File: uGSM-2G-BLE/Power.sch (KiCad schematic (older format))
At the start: 11 parts

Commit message: power
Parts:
- added C? (x3): 100nF, Capacitor_SMD:C_0603_1608Metric, symbol Device:C
- added C?: 1uF, Capacitor_SMD:C_0603_1608Metric, symbol Device:C
- added C?: 2.2uF, Capacitor_SMD:C_0603_1608Metric, symbol Device:C
- added C?: 10uF, Capacitor_SMD:C_0603_1608Metric, symbol Device:C
- added D?: D, symbol Device:D
- added D?: PRTR5V0U2X, Package_TO_SOT_SMD:SOT-143, symbol Power_Protection:PRTR5V0U2X
- added J?: VCC_INPUT, symbol Connector:Screw_Terminal_01x02
- added J?: USB_B_Micro, symbol Connector:USB_B_Micro
- added U?: MIC5225-3.3YM5-TR, Package_TO_SOT_SMD:SOT-23-5, symbol Regulator_Linear:MIC5205-3.3YM5
- U?: Manufacturerpart (none) -> TPS562201DDCR
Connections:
- net GND: now also C?.2, C?.2, C?.2, C?.2, C?.2, C?.2, D?.1 (GND), J?.1 (Pin_1), J?.5 (GND), J?.6 (Shield), U?.2 (GND)
- net SIM_VCC: now also C?.1, U?.1 (IN), U?.3 (EN)
- net VCC: now also D?.1 (K), J?.2 (Pin_2)
- new net 3V3: C?.1, U?.5 (OUT)
- new net USB_5V: C?.1, C?.1, C?.1, C?.1, D?.2 (A), D?.4 (VCC), J?.1 (VBUS)
- new net USB_D+: D?.3 (I/O2), J?.3 (D+)
- new net USB_D-: D?.2 (I/O1), J?.2 (D-)
- no-connect marks 0 -> 2
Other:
- note added: "Atleast 16V rated cap"
- note added: "Follow classic USB guidelines"
- note added: "May change! Check issue on github"
- note added: "R1 and R2 +/- 1%\n"

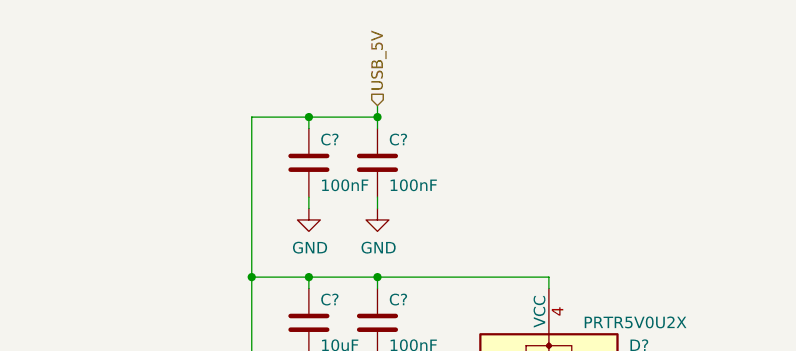
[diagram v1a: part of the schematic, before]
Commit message: ble connected to mikrobus
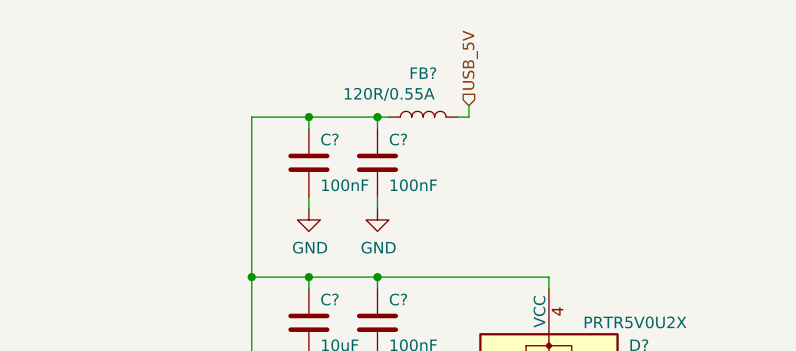
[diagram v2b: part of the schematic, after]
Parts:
- added FB?: 120R/0.55A, symbol Device:L
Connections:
- net USB_5V: now also FB?.2; no longer C?.1, C?.1, C?.1, C?.1, D?.4 (VCC), J?.1 (VBUS)
- new net: C?.1, C?.1, C?.1, C?.1, D?.4 (VCC), FB?.1, J?.1 (VBUS)
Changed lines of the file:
@@
 $Descr A4 11693 8268
 encoding utf-8
-Sheet 3 6
+Sheet 2 6
 Title ""
 Date ""
@@
 $EndComp
 $Comp
-L power:GND #PWR?
-U 1 1 5E5196D5
-P 8450 3750
-F 0 "#PWR?" H 8450 3500 50  0001 C CNN
-F 1 "GND" H 8455 3577 50  0000 C CNN
-F 2 "" H 8450 3750 50  0001 C CNN
-F 3 "" H 8450 3750 50  0001 C CNN
-	1    8450 3750
-	1    0    0    -1
-$EndComp
-Wire Wire Line
-	8400 3650 8400 3700
-Wire Wire Line
-	8400 3700 8450 3700
-Wire Wire Line
-	8500 3700 8500 3650
-Wire Wire Line
-	8450 3700 8450 3750
-Connection ~ 8450 3700
-Wire Wire Line
-	8450 3700 8500 3700
-$Comp
 L Power_Protection:PRTR5V0U2X D?
 U 1 1 5E51C285
@@
 Wire Wire Line
 	8850 1050 9100 1050
-Wire Wire Line
-	9400 1050 9400 1000
 Connection ~ 8850 1750
 Wire Wire Line
 	9400 1050 9400 1100
-Connection ~ 9400 1050
 Wire Wire Line
 	9100 1050 9100 1100
@@
 Wire Wire Line
 	9400 1400 9400 1450
-Text HLabel 9400 1000 1    50   Input ~ 0
+Text HLabel 9800 1000 1    50   Input ~ 0
 USB_5V
 Text Notes 9650 3500 0    50   ~ 0
@@
 Wire Wire Line
 	5650 3550 5700 3550
+$Comp
+L Device:L FB?
+U 1 1 5E54216F
+P 9600 1050
+F 0 "FB?" V 9790 1050 50  0000 C CNN
+F 1 "120R/0.55A" V 9700 1200 50  0000 C CNN
+F 2 "" H 9600 1050 50  0001 C CNN
+F 3 "~" H 9600 1050 50  0001 C CNN
+	1    9600 1050
+	0    -1   -1   0
+$EndComp
+Wire Wire Line
+	9450 1050 9400 1050
+Connection ~ 9400 1050
+Wire Wire Line
+	9750 1050 9800 1050
+Wire Wire Line
+	9800 1050 9800 1000
+Wire Wire Line
+	8450 3700 8500 3700
+Wire Wire Line
+	8500 3700 8500 3650
+Wire Wire Line
+	8400 3650 8400 3700
+$Comp
+L power:GND #PWR?
+U 1 1 5E5196D5
+P 8450 3750
+F 0 "#PWR?" H 8450 3500 50  0001 C CNN
+F 1 "GND" H 8455 3577 50  0000 C CNN
+F 2 "" H 8450 3750 50  0001 C CNN
+F 3 "" H 8450 3750 50  0001 C CNN
+	1    8450 3750
+	1    0    0    -1
+$EndComp
+Wire Wire Line
+	8450 3700 8450 3750
+Connection ~ 8450 3700
+Wire Wire Line
+	8400 3700 8450 3700
 $EndSCHEMATC

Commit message: completed all issues, updating
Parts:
- removed C? (x3): 100nF, Capacitor_SMD:C_0603_1608Metric, symbol Device:C
- removed C?: 1uF, Capacitor_SMD:C_0603_1608Metric, symbol Device:C
- removed C?: 2.2uF, Capacitor_SMD:C_0603_1608Metric, symbol Device:C
- removed C?: 10uF, Capacitor_SMD:C_0603_1608Metric, symbol Device:C
- removed D?: D, symbol Device:D
- removed D?: PRTR5V0U2X, Package_TO_SOT_SMD:SOT-143, symbol Power_Protection:PRTR5V0U2X
- removed FB?: 120R/0.55A, symbol Device:L
- removed J?: VCC_INPUT, symbol Connector:Screw_Terminal_01x02
- removed U?: MIC5225-3.3YM5-TR, Package_TO_SOT_SMD:SOT-23-5, symbol Regulator_Linear:MIC5205-3.3YM5
- added C? (x2): 10uF, Capacitor_SMD:C_0805_2012Metric, symbol Device:C
- added C? (x2): 100nF, Capacitor_SMD:C_0603_1608Metric, symbol Device:C
- added C?: 330pF, Capacitor_SMD:C_0603_1608Metric, symbol Device:C
- added D?: MBR120, Diode_SMD:D_SOD-123F, symbol Diode:MBR340
- added J?: PWR_INPUT, symbol Connector:Screw_Terminal_01x02
- added L?: BLM21PG220SN1D, Inductor_SMD:L_0805_2012Metric, symbol Device:L
- added Q?: DMG2305, Package_TO_SOT_SMD:SOT-23, symbol Transistor_FET:DMG2301L
- added R? (x2): 100K, Resistor_SMD:R_0603_1608Metric, symbol Device:R
- added R?: 1M, Resistor_SMD:R_0603_1608Metric, symbol Device:R
- added R? (x2): 27, Resistor_SMD:R_0603_1608Metric, symbol Device:R
- added U?: AP2112K-3.3, Package_TO_SOT_SMD:SOT-23-5, symbol Regulator_Linear:AP2112K-3.3
- added U?: USBLC6-2SC6, Package_TO_SOT_SMD:SOT-23-6, symbol Power_Protection:USBLC6-2SC6
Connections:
- net 3V3: now also C?.1, U?.5 (VOUT)
- net GND: now also C?.1, C?.1, C?.1, C?.2, C?.2, J?.1 (Pin_1), R?.1, R?.1, U?.2 (GND), U?.2 (GND); no longer J?.6 (Shield)
- net USB_5V: now also C?.2, D?.2 (A), L?.1, Q?.1 (G), R?.2, U?.5 (VBUS)
- net USB_D+: now also R?.2; no longer J?.3 (D+)
- net USB_D-: now also R?.2; no longer J?.2 (D-)
- net VCC: now also C?.1, D?.1 (K), Q?.2 (S), R?.2, U?.1 (VIN)
- net at J?.1 (VBUS): now also C?.2, L?.2
- new net: C?.2, J?.6 (Shield), R?.2
- new net: R?.1, U?.3 (EN)
- new net: R?.1, U?.4 (IO2)
- new net: R?.1, U?.6 (IO1)
- new net PWR_USB_D+: J?.3 (D+), U?.3 (IO2)
- new net PWR_USB_D-: J?.2 (D-), U?.1 (IO1)
- new net RAW_PWR_IN: J?.2 (Pin_2), Q?.3 (D)
- no-connect marks 2 -> 1
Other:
- note added: "select footprint\n"
- note removed: "Atleast 16V rated cap"
- note removed: "Follow classic USB guidelines"
- note removed: "May change! Check issue on github"
- moved on the sheet: J?

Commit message: added all email issue correction
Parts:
- removed Q?: DMG2305, Package_TO_SOT_SMD:SOT-23, symbol Transistor_FET:DMG2301L
- removed R?: 27, Resistor_SMD:R_0603_1608Metric, symbol Device:R
- removed U?: USBLC6-2SC6, Package_TO_SOT_SMD:SOT-23-6, symbol Power_Protection:USBLC6-2SC6
- added Q?: DMG2305, Package_TO_SOT_SMD:SOT-23, symbol Transistor_FET:SUD08P06-155L
- added R?: 27, Resistor_SMD:R_0603_1608Metric, symbol Device:R
- added U?: USBLC6, symbol ugsm_lib:USBLC6
- R?: value 100K -> 10K
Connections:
- net GND: now also U?.2 (GND)
- net PWR_USB_D+: now also U?.3 (INPUT2)
- net PWR_USB_D-: now also U?.1 (INPUT1)
- net RAW_PWR_IN: now also Q?.2 (D)
- net USB_5V: now also Q?.1 (G), U?.5 (VCC)
- net USB_D+: now also R?.2
- net VCC: now also Q?.3 (S)
- net at R?.1: now also U?.6 (OUTPUT1)
- new net: R?.1, U?.4 (OUTPUT2)
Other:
- moved on the sheet: R?
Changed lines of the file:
@@
 $EndComp
 NoConn ~ 7600 1950
-Text HLabel 9000 1350 1    50   Input ~ 0
+Text HLabel 10800 1700 2    50   Input ~ 0
 USB_D-
-Text HLabel 10100 1400 1    50   Input ~ 0
+Text HLabel 10800 1850 2    50   Input ~ 0
 USB_D+
 Text HLabel 8600 1500 1    50   Input ~ 0
@@
 3V3
 $Comp
-L Transistor_FET:DMG2301L Q?
-U 1 1 5E80CE9A
-P 1300 3600
-F 0 "Q?" H 1504 3646 50  0000 L CNN
-F 1 "DMG2305" H 1504 3555 50  0000 L CNN
-F 2 "Package_TO_SOT_SMD:SOT-23" H 1500 3525 50  0001 L CIN
-F 3 "https://www.diodes.com/assets/Datasheets/DMG2305UX.pdf" H 1300 3600 50  0001 L CNN
-	1    1300 3600
-	1    0    0    -1
-$EndComp
-$Comp
 L Diode:MBR340 D?
 U 1 1 5E80DF50
@@
 P 1000 4300
 F 0 "R?" H 950 4350 50  0000 R CNN
-F 1 "100K" H 950 4450 50  0000 R CNN
+F 1 "10K" H 950 4450 50  0000 R CNN
 F 2 "Resistor_SMD:R_0603_1608Metric" V 930 4300 50  0001 C CNN
 F 3 "~" H 1000 4300 50  0001 C CNN
@@
 Text GLabel 1400 3250 1    50   Input ~ 0
 RAW_PWR_IN
-$Comp
-L Power_Protection:USBLC6-2SC6 U?
-U 1 1 5E8934D8
-P 9550 1950
-F 0 "U?" H 9300 2300 50  0000 C CNN
-F 1 "USBLC6-2SC6" H 9950 1600 50  0000 C CNN
-F 2 "Package_TO_SOT_SMD:SOT-23-6" H 8800 2350 50  0001 C CNN
-F 3 "http://www2.st.com/resource/en/datasheet/CD00050750.pdf" H 9750 2300 50  0001 C CNN
-F 4 "https://export.farnell.com/stmicroelectronics/usblc6-2sc6/esd-protection-3-5pf-17v-sot23/dp/1269406?st=USBLC6-2" H 9550 1950 50  0001 C CNN "Farnell"
-	1    9550 1950
-	1    0    0    -1
-$EndComp
 $Comp
 L Device:C C?
@@
 L Device:R R?
 U 1 1 5E8A0288
-P 9000 1550
-F 0 "R?" H 8950 1600 50  0000 R CNN
-F 1 "27" H 8950 1700 50  0000 R CNN
-F 2 "Resistor_SMD:R_0603_1608Metric" V 8930 1550 50  0001 C CNN
-F 3 "~" H 9000 1550 50  0001 C CNN
-	1    9000 1550
-	-1   0    0    1
-$EndComp
-$Comp
-L Device:R R?
-U 1 1 5E8A077E
-P 10100 1600
-F 0 "R?" H 10050 1650 50  0000 R CNN
-F 1 "27" H 10050 1750 50  0000 R CNN
-F 2 "Resistor_SMD:R_0603_1608Metric" V 10030 1600 50  0001 C CNN
-F 3 "~" H 10100 1600 50  0001 C CNN
-	1    10100 1600
-	-1   0    0    1
+P 10600 1700
+F 0 "R?" V 10600 1750 50  0000 R CNN
+F 1 "27" V 10650 1600 50  0000 R CNN
+F 2 "Resistor_SMD:R_0603_1608Metric" V 10530 1700 50  0001 C CNN
+F 3 "~" H 10600 1700 50  0001 C CNN
+	1    10600 1700
+	0    -1   -1   0
 $EndComp
 Wire Wire Line
@@
 Wire Wire Line
 	8600 1550 8600 1500
-Text HLabel 9550 1400 1    50   Input ~ 0
+Text HLabel 9850 1400 1    50   Input ~ 0
 USB_5V
-$Comp
-L power:GND #PWR?
-U 1 1 5E8E108F
-P 9550 2500
-F 0 "#PWR?" H 9550 2250 50  0001 C CNN
-F 1 "GND" H 9555 2327 50  0000 C CNN
-F 2 "" H 9550 2500 50  0001 C CNN
-F 3 "" H 9550 2500 50  0001 C CNN
-	1    9550 2500
-	1    0    0    -1
-$EndComp
-Wire Wire Line
-	9550 1400 9550 1450
-Wire Wire Line
-	9550 2450 9550 2500
 Text GLabel 7650 1750 2    50   Input ~ 0
 PWR_USB_D+
@@
 	7600 1850 7650 1850
 Connection ~ 8200 1550
-Text GLabel 9000 2050 0    50   Input ~ 0
+Text GLabel 9250 1700 0    50   Input ~ 0
 PWR_USB_D-
-Text GLabel 10100 2050 2    50   Input ~ 0
+Text GLabel 9250 1850 0    50   Input ~ 0
 PWR_USB_D+
-Wire Wire Line
-	9000 1700 9000 1850
-Wire Wire Line
-	9000 1850 9050 1850
-Wire Wire Line
-	9000 2050 9050 2050
-Wire Wire Line
-	9000 1350 9000 1400
-Wire Wire Line
-	10100 1400 10100 1450
-Wire Wire Line
-	10050 1850 10100 1850
-Wire Wire Line
-	10100 1850 10100 1750
-Wire Wire Line
-	10050 2050 10100 2050
+$Comp
+L Transistor_FET:SUD08P06-155L Q?
+U 1 1 5E6AE7AF
+P 1300 3600
+F 0 "Q?" H 1504 3646 50  0000 L CNN
+F 1 "DMG2305" H 1504 3555 50  0000 L CNN
+F 2 "Package_TO_SOT_SMD:SOT-23" H 1500 3525 50  0001 L CIN
+F 3 "https://www.diodes.com/assets/Datasheets/DMG2305UX.pdf" H 1300 3600 50  0001 L CNN
+	1    1300 3600
+	1    0    0    -1
+$EndComp
+$Comp
+L ugsm_lib:USBLC6 U?
+U 1 1 5E73108B
+P 9850 1800
+F 0 "U?" H 10250 2100 50  0000 C CNN
+F 1 "USBLC6" H 9500 2100 50  0000 C CNN
+F 2 "" H 9600 2000 50  0001 C CNN
+F 3 "" H 9600 2000 50  0001 C CNN
+	1    9850 1800
+	1    0    0    -1
+$EndComp
+$Comp
+L Device:R R?
+U 1 1 5E747AA3
+P 10600 1850
+F 0 "R?" V 10600 1900 50  0000 R CNN
+F 1 "27" V 10650 1750 50  0000 R CNN
+F 2 "Resistor_SMD:R_0603_1608Metric" V 10530 1850 50  0001 C CNN
+F 3 "~" H 10600 1850 50  0001 C CNN
+	1    10600 1850
+	0    -1   -1   0
+$EndComp
+$Comp
+L power:GND #PWR?
+U 1 1 5E74FC44
+P 9850 2150
+F 0 "#PWR?" H 9850 1900 50  0001 C CNN
+F 1 "GND" H 9855 1977 50  0000 C CNN
+F 2 "" H 9850 2150 50  0001 C CNN
+F 3 "" H 9850 2150 50  0001 C CNN
+	1    9850 2150
+	1    0    0    -1
+$EndComp
+Wire Wire Line
+	9250 1700 9300 1700
+Wire Wire Line
+	9250 1850 9300 1850
+Wire Wire Line
+	9850 1400 9850 1450
+Wire Wire Line
+	9850 2100 9850 2150
+Wire Wire Line
+	10400 1700 10450 1700
+Wire Wire Line
+	10400 1850 10450 1850
+Wire Wire Line
+	10750 1700 10800 1700
+Wire Wire Line
+	10750 1850 10800 1850
 $EndSCHEMATC
